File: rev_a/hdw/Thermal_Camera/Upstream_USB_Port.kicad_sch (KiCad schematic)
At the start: 15 parts

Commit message: added some more USB stuff
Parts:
- removed C?: 0.1uF, Capacitors_SMD:C_0603, symbol Custom_Library:C_Custom
- added C? (x3): 10uF, Capacitors_SMD:C_0603, symbol Custom_Library:C_Custom
- added C?: 0.1uF, Capacitors_SMD:C_0603, symbol Custom_Library:C_Custom
- added C?: 10uF, Capacitors_SMD:C_1206, symbol Custom_Library:C_Custom
- added R?: 3.57k, Resistors_SMD:R_0603, symbol Custom_Library:R_Custom
- added R?: 1.15k, Resistors_SMD:R_0603, symbol Custom_Library:R_Custom
- added R?: 10k, Resistors_SMD:R_0603, symbol Custom_Library:R_Custom
- added TP?: TP, Custom Footprints Library:Test_Point, symbol Custom_Library:TP
- added U?: TPS7A92, Package_DFN_QFN:Texas_S-PDSO-N10_EP1.2x2mm, symbol Custom_Library:TPS7A91
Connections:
- net +3.3V_USB: now also C?.1, C?.1, R?.1, R?.1, TP?.1 (TP), U?.1 (OUT), U?.2 (OUT); no longer C?.1, R?.1, U?.5 (Vs)
- net +5V_USB: now also C?.1, R?.1, U?.5 (Vs), C?.1, C?.1, U?.10 (IN), U?.6 (SS_CTRL), U?.9 (IN)
- net GND: now also C?.2, C?.2, C?.2, C?.2, C?.2, R?.2, U?.11 (GND), U?.4 (GND)
- net POS5_USB_PGOOD: now also U?.7 (EN)
- new net: R?.1, R?.2, U?.3 (FB)
- new net: C?.1, U?.8 (NR/SS)
- new net POS3P3_USB_PGOOD: R?.2, U?.5 (PG)
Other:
- moved on the sheet: C?, R?, U?

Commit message: chose backlight boost inductor
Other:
- company: (none) -> Drew Maatman and Michael Laffin
- title: (none) -> Thermal Camera
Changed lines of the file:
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@@
 (kicad_sch (version 20230121) (generator eeschema)
-  (paper "A4")
+  (paper "A")
+  (title_block
+    (title "Thermal Camera")
+    (date "2023-12-07")
+    (rev "PRELIM")
+    (company "Drew Maatman and Michael Laffin")
+  )
   (junction (at 260.35 124.46) (diameter 0) (color 0 0 0 0)
   )

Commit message: lots of random schematic progress
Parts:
- removed C?: 0.1uF, Capacitors_SMD:C_0603, symbol Custom_Library:C_Custom
- removed R?: 487k, Resistors_SMD:R_0603, symbol Custom_Library:R_Custom
- removed R?: 6.04k, Resistors_SMD:R_0603, symbol Custom_Library:R_Custom
- removed R?: 10k, Resistors_SMD:R_0603, symbol Custom_Library:R_Custom
- removed R?: 40.2k, Resistors_SMD:R_0603, symbol Custom_Library:R_Custom
- removed U?: TLV6700, Package_TO_SOT_SMD:SOT-23-6, symbol Custom_Library:TLV6700
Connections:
- net POS5_USB_PGOOD is gone; now on net +5V_USB: U?.7 (EN)
- net +5V_USB: no longer U?.6 (SS_CTRL)
- net GND: now also U?.6 (SS_CTRL)
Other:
- moved on the sheet: C?, R?, TP?, U?

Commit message: blah blah
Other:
- moved on the sheet: C?, R?, TP?, U?

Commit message: lots of schematic progress
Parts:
- C2601, C2603, C2605: renamed from C?; footprint Capacitors_SMD:C_0603 -> (none); Digi-Key PN 399-8153-1-ND -> (none); display_footprint 0603 -> (none)
- C2602: renamed from C?; footprint Capacitors_SMD:C_0603 -> (none); Digi-Key PN 1276-1935-1-ND -> (none); display_footprint 0603 -> (none)
- C2604, C2606: renamed from C?; footprint Capacitors_SMD:C_0603 -> (none); Digi-Key PN 1292-1501-1-ND -> (none); display_footprint 0603 -> (none)
- R2602, R2603: renamed from R?; footprint Resistors_SMD:R_0603 -> (none); Digi-Key PN 541-27.0HCT-ND -> (none); Wattage 1/10W -> (none); display_footprint 0603 -> (none)
- R2604, R2606: renamed from R?; footprint Resistors_SMD:R_0603 -> (none); Wattage 1/10W -> (none); display_footprint 0603 -> (none)
- R2605: renamed from R?; footprint Resistors_SMD:R_0603 -> (none); Digi-Key PN 541-1.15KHCT-ND -> (none); Wattage 1/10W -> (none); display_footprint 0603 -> (none)
- R?: footprint Resistors_SMD:R_0603 -> (none); Digi-Key PN 541-10.0KHCT-ND -> (none); Wattage 1/10W -> (none); display_footprint 0603 -> (none)
- gave numbers to parts that had none: 6

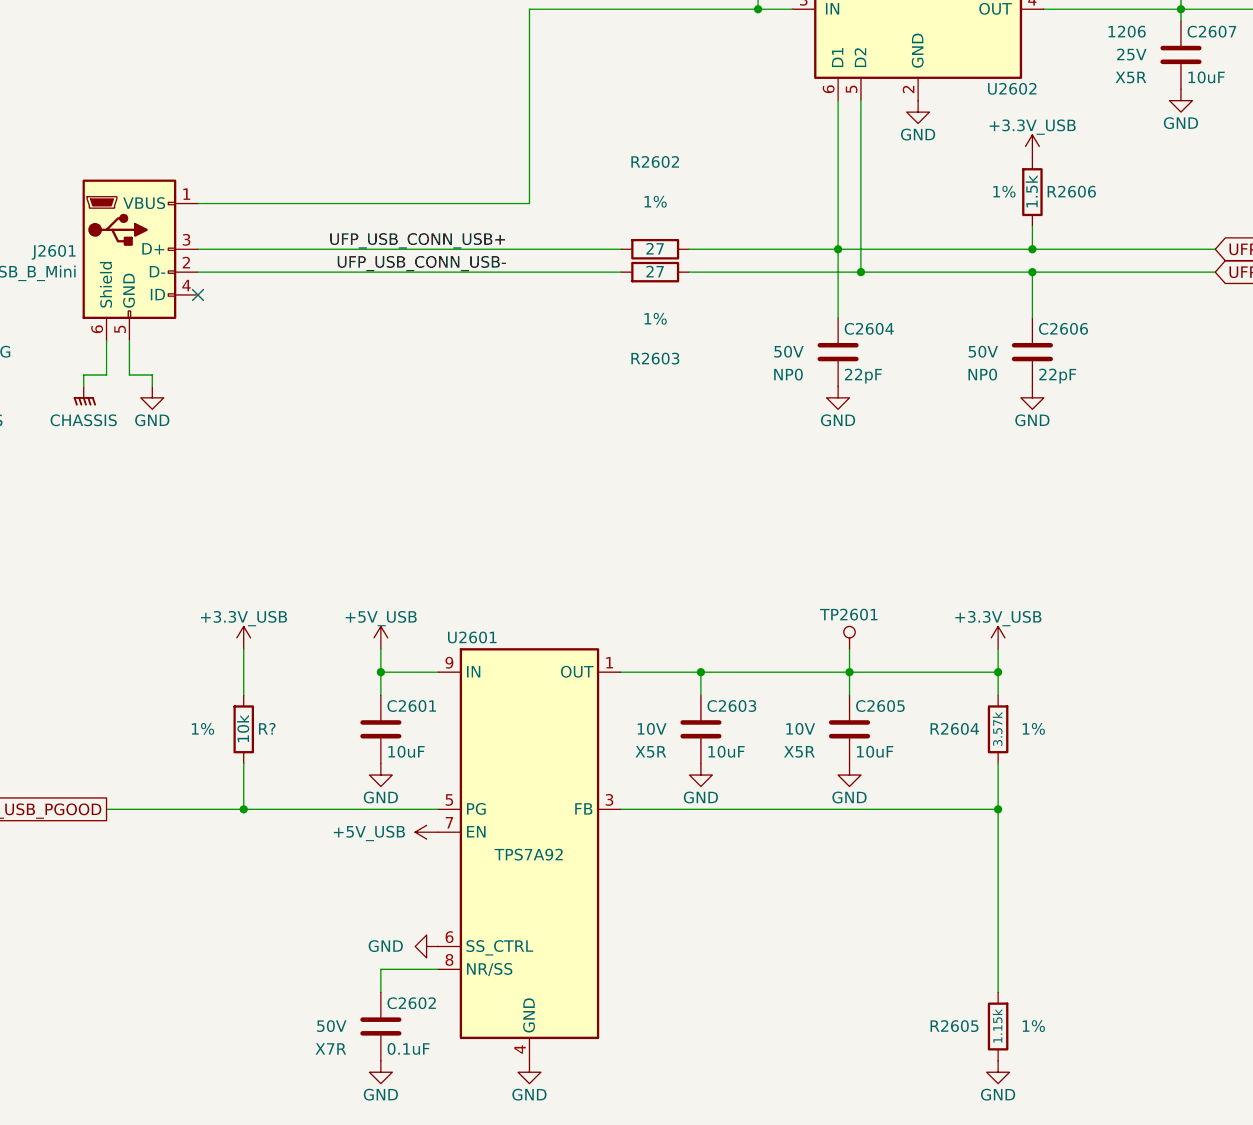
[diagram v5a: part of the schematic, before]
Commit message: assigned a ton of footprints
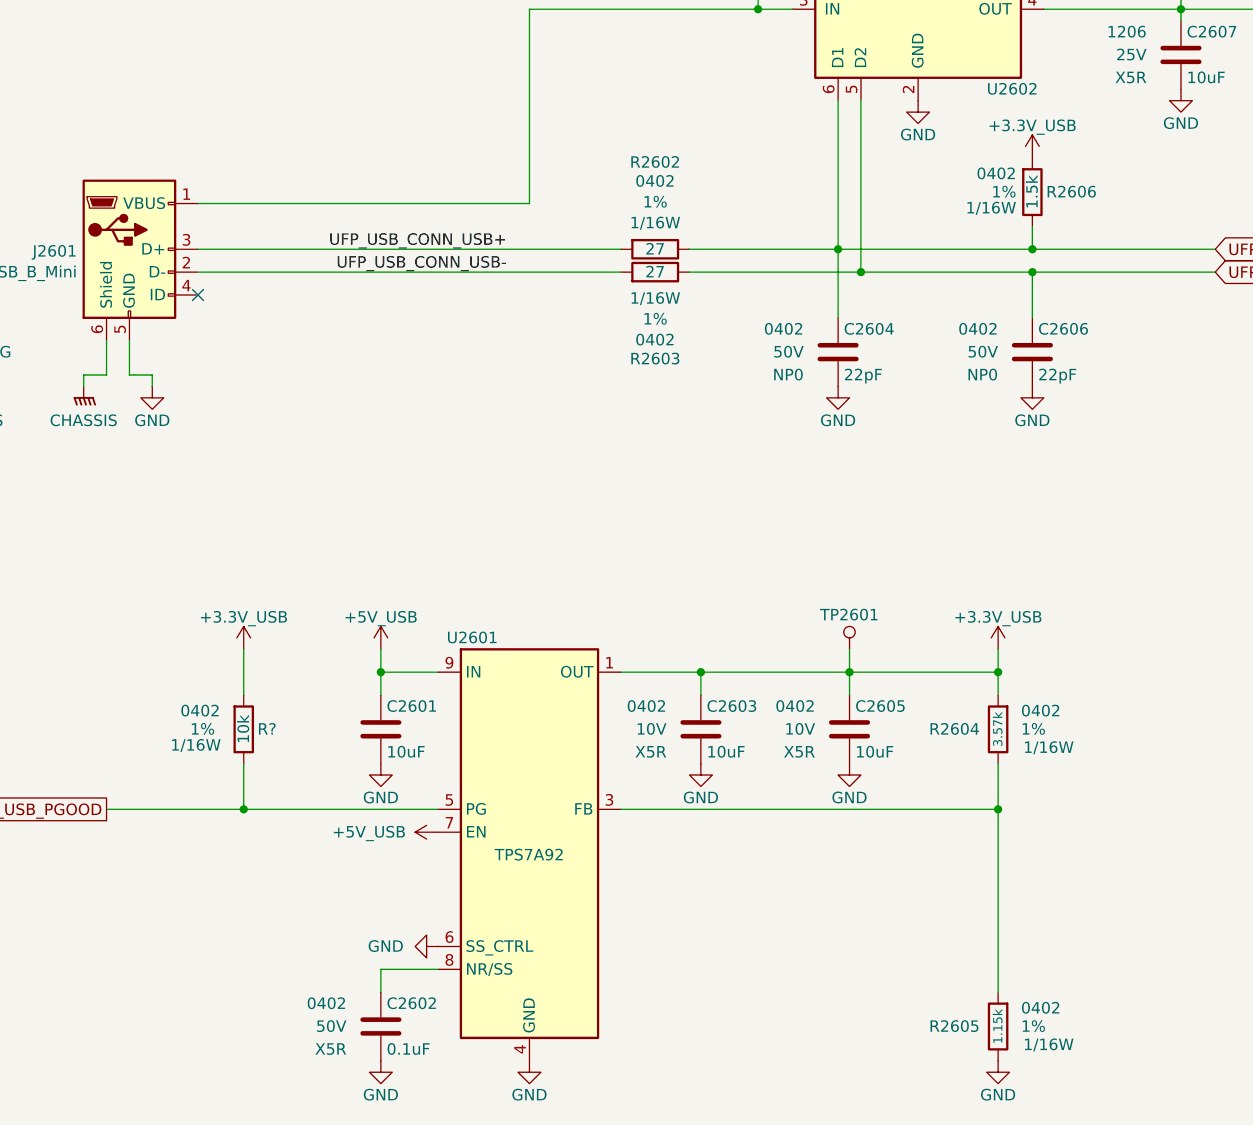
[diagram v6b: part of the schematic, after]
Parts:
- C2601, C2603, C2604, C2605, C2606: footprint (none) -> Capacitors_SMD:C_0402; display_footprint (none) -> 0402
- C2602: footprint (none) -> Capacitors_SMD:C_0402; Dielectric X7R -> X5R; display_footprint (none) -> 0402
- R2602, R2603, R2604, R2605, R2606, R?: footprint (none) -> Resistors_SMD:R_0402; Wattage (none) -> 1/16W; display_footprint (none) -> 0402
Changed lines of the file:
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@@
 			)
 		)
-		(property "Footprint" ""
+		(property "Footprint" "Resistors_SMD:R_0402"
 			(at 177.8 55.88 0)
 			(effects
@@
 			)
 		)
-		(property "display_footprint" ""
+		(property "display_footprint" "0402"
 			(at 176.022 53.848 0)
 			(effects
@@
 			)
 		)
-		(property "Wattage" ""
+		(property "Wattage" "1/16W"
 			(at 176.022 57.658 0)
 			(effects
@@
 			)
 		)
-		(property "Footprint" ""
+		(property "Footprint" "Resistors_SMD:R_0402"
 			(at 173.99 115.57 0)
 			(effects
@@
 			)
 		)
-		(property "display_footprint" ""
+		(property "display_footprint" "0402"
 			(at 176.53 113.538 0)
 			(effects
@@
 			)
 		)
-		(property "Wattage" ""
+		(property "Wattage" "1/16W"
 			(at 176.784 117.602 0)
 			(effects
@@
 			)
 		)
-		(property "Footprint" ""
+		(property "Footprint" "Capacitors_SMD:C_0402"
 			(at 106.3752 119.38 0)
 			(effects
@@
 			)
 		)
-		(property "display_footprint" ""
+		(property "display_footprint" "0402"
 			(at 101.6 113.665 0)
 			(effects
@@
 			)
 		)
-		(property "Footprint" ""
+		(property "Footprint" "Resistors_SMD:R_0402"
 			(at 135.89 62.23 0)
 			(effects
@@
 			)
 		)
-		(property "display_footprint" ""
+		(property "display_footprint" "0402"
 			(at 135.89 54.6862 90)
 			(effects
@@
 			)
 		)
-		(property "Wattage" ""
+		(property "Wattage" "1/16W"
 			(at 135.89 59.309 90)
 			(effects
@@
 			)
 		)
-		(property "Footprint" ""
+		(property "Footprint" "Resistors_SMD:R_0402"
 			(at 135.89 64.77 0)
 			(effects
@@
 			)
 		)
-		(property "display_footprint" ""
+		(property "display_footprint" "0402"
 			(at 135.89 72.3138 90)
 			(effects
@@
 			)
 		)
-		(property "Wattage" ""
+		(property "Wattage" "1/16W"
 			(at 135.89 67.691 90)
 			(effects
@@
 			)
 		)
-		(property "Footprint" ""
+		(property "Footprint" "Capacitors_SMD:C_0402"
 			(at 141.9352 119.38 0)
 			(effects
@@
 			)
 		)
-		(property "display_footprint" ""
+		(property "display_footprint" "0402"
 			(at 137.16 113.03 0)
 			(effects
@@
 			)
 		)
-		(property "Footprint" ""
+		(property "Footprint" "Capacitors_SMD:C_0402"
 			(at 157.1752 77.47 0)
 			(effects
@@
 			)
 		)
-		(property "display_footprint" ""
+		(property "display_footprint" "0402"
 			(at 152.4 71.12 0)
 			(effects
@@
 			)
 		)
-		(property "Footprint" ""
+		(property "Footprint" "Capacitors_SMD:C_0402"
 			(at 106.3752 152.4 0)
 			(effects
@@
 			)
 		)
-		(property "display_footprint" ""
+		(property "display_footprint" "0402"
 			(at 101.6 146.05 0)
 			(effects
@@
 			)
 		)
-		(property "Dielectric" "X7R"
+		(property "Dielectric" "X5R"
 			(at 101.6 151.13 0)
 			(effects
@@
 			)
 		)
-		(property "Footprint" ""
+		(property "Footprint" "Capacitors_SMD:C_0402"
 			(at 158.4452 119.38 0)
 			(effects
@@
 			)
 		)
-		(property "display_footprint" ""
+		(property "display_footprint" "0402"
 			(at 153.67 113.03 0)
 			(effects
@@
 			)
 		)
-		(property "Footprint" ""
+		(property "Footprint" "Resistors_SMD:R_0402"
 			(at 173.99 148.59 0)
 			(effects
@@
 			)
 		)
-		(property "display_footprint" ""
+		(property "display_footprint" "0402"
 			(at 176.53 146.558 0)
 			(effects
@@
 			)
 		)
-		(property "Wattage" ""
+		(property "Wattage" "1/16W"
 			(at 176.784 150.622 0)
 			(effects
@@
 			)
 		)
-		(property "Footprint" ""
+		(property "Footprint" "Capacitors_SMD:C_0402"
 			(at 178.7652 77.47 0)
 			(effects
@@
 			)
 		)
-		(property "display_footprint" ""
+		(property "display_footprint" "0402"
 			(at 173.99 71.12 0)
 			(effects
@@
 			)
 		)
-		(property "Footprint" ""
+		(property "Footprint" "Resistors_SMD:R_0402"
 			(at 90.17 115.57 0)
 			(effects
@@
 			)
 		)
-		(property "display_footprint" ""
+		(property "display_footprint" "0402"
 			(at 85.344 113.538 0)
 			(effects
@@
 			)
 		)
-		(property "Wattage" ""
+		(property "Wattage" "1/16W"
 			(at 84.836 117.348 0)
 			(effects

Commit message: assigned some part numbers
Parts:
- C2601, C2603, C2605: Digi-Key PN (none) -> 490-GRM155R61A106ME11DCT-ND
- C2602: Digi-Key PN (none) -> 490-10697-1-ND
- C2604, C2606: Digi-Key PN (none) -> 490-5868-1-ND
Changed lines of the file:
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@@
 			)
 		)
-		(property "Digi-Key PN" ""
+		(property "Digi-Key PN" "490-GRM155R61A106ME11DCT-ND"
 			(at 105.41 115.57 0)
 			(effects
@@
 			)
 		)
-		(property "Digi-Key PN" ""
+		(property "Digi-Key PN" "490-GRM155R61A106ME11DCT-ND"
 			(at 140.97 115.57 0)
 			(effects
@@
 			)
 		)
-		(property "Digi-Key PN" ""
+		(property "Digi-Key PN" "490-5868-1-ND"
 			(at 156.21 73.66 0)
 			(effects
@@
 			)
 		)
-		(property "Digi-Key PN" ""
+		(property "Digi-Key PN" "490-10697-1-ND"
 			(at 116.205 135.89 0)
 			(effects
@@
 			)
 		)
-		(property "Digi-Key PN" ""
+		(property "Digi-Key PN" "490-GRM155R61A106ME11DCT-ND"
 			(at 157.48 115.57 0)
 			(effects
@@
 			)
 		)
-		(property "Digi-Key PN" ""
+		(property "Digi-Key PN" "490-5868-1-ND"
 			(at 177.8 73.66 0)
 			(effects

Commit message: assigned resistor part numbers
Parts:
- R2602, R2603: Digi-Key PN (none) -> RMCF0402FT27R0CT-ND
- R2604: Digi-Key PN (none) -> RMCF0402FT3K57CT-ND
- R2605: Digi-Key PN (none) -> RMCF0402FT1K15CT-ND
- R2606: Digi-Key PN (none) -> RMCF0402FT1K50CT-ND
- R?: Digi-Key PN (none) -> RMCF0402FT10K0CT-ND
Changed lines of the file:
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@@
 			)
 		)
-		(property "Digi-Key PN" ""
+		(property "Digi-Key PN" "RMCF0402FT1K50CT-ND"
 			(at 177.8 55.88 0)
 			(effects
@@
 			)
 		)
-		(property "Digi-Key PN" ""
+		(property "Digi-Key PN" "RMCF0402FT3K57CT-ND"
 			(at 173.99 115.57 0)
 			(effects
@@
 			)
 		)
-		(property "Digi-Key PN" ""
+		(property "Digi-Key PN" "RMCF0402FT27R0CT-ND"
 			(at 125.73 54.61 0)
 			(effects
@@
 			)
 		)
-		(property "Digi-Key PN" ""
+		(property "Digi-Key PN" "RMCF0402FT27R0CT-ND"
 			(at 125.73 72.39 0)
 			(effects
@@
 			)
 		)
-		(property "Digi-Key PN" ""
+		(property "Digi-Key PN" "RMCF0402FT1K15CT-ND"
 			(at 173.99 148.59 0)
 			(effects
@@
 			)
 		)
-		(property "Digi-Key PN" ""
+		(property "Digi-Key PN" "RMCF0402FT10K0CT-ND"
 			(at 82.55 105.41 0)
 			(effects
